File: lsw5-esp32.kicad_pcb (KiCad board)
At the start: 2 copper layers, 35 x 52 mm, 36 parts, among them J1 Conn_02x03_Odd_Even, J2 Conn_01x04_Pin, J3 USB4105-GF-A, J4 Conn_02x05_Odd_Even, J6 Conn_01x04, Q1 AO3407A, U1 ESP32-S3-WROOM-1U, U2 LD1117S33TR_SOT223, U3 ISO1410DWR

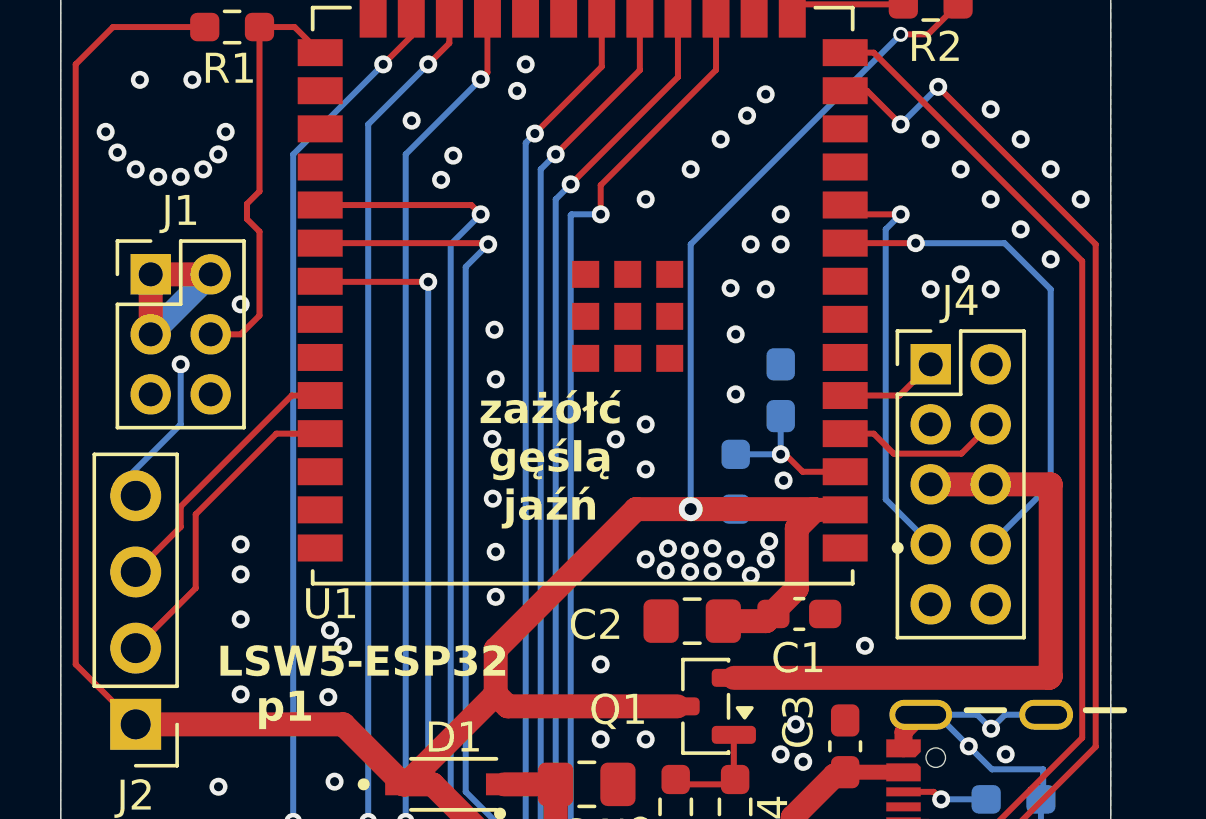
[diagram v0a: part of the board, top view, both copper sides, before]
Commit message: Fix pin header footprint being on the wrong side, not that it matters for THT but to have a reasonable render
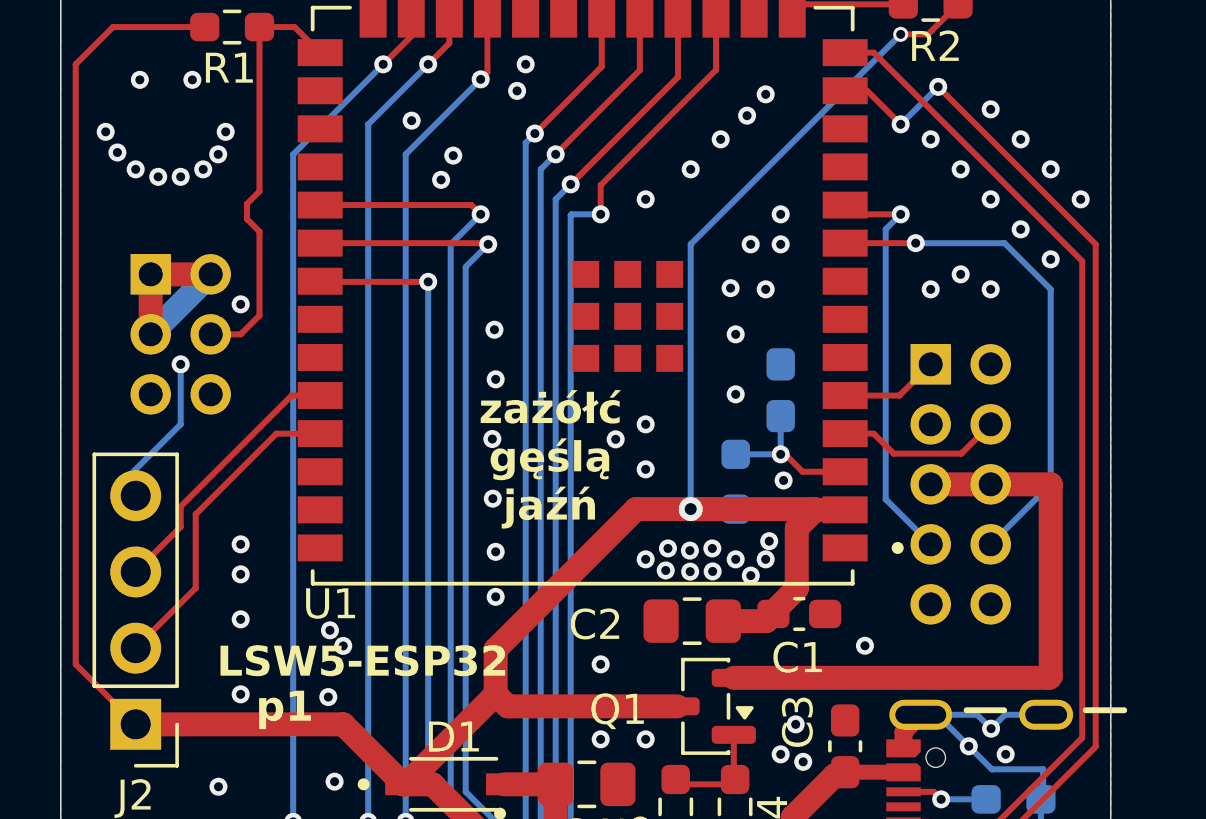
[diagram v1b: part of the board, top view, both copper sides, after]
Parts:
- J1, J4: moved to B.Cu
- moved J1 2.00 mm to (5.00, 11.0), turned to 180 degrees
- moved J4 2.00 mm to (31.0, 14.0), turned to 180 degrees

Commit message: Fix LED labels on silkscreen
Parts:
- D2: value COM -> NET
- D4: value NET -> COM
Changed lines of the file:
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@@
 	(title_block
 		(title "LSW5-ESP32")
-		(rev "p1")
+		(rev "p2")
 	)
 	(layers
@@
 			)
 		)
-		(property "Value" "COM"
+		(property "Value" "NET"
 			(at 0 -1.492775 0)
 			(layer "F.SilkS")
@@
 			)
 		)
-		(property "Value" "NET"
+		(property "Value" "COM"
 			(at 0 -1.492775 0)
 			(layer "F.SilkS")

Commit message: RS485 series resistors to 0Ω
To be removed in p2? Also, putting the series resistors before the 120Ω
termination is bad, not that any of these considerations *probably*
matter for chassis wiring
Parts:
- R13, R6: value 10 -> 0
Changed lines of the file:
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@@
 			)
 		)
-		(property "Value" "10"
+		(property "Value" "0"
 			(at 0 1.43 0)
 			(layer "F.Fab")
@@
 			)
 		)
-		(property "Value" "10"
+		(property "Value" "0"
 			(at 0 1.43 0)
 			(layer "F.Fab")
